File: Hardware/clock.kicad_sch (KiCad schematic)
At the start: 0 parts

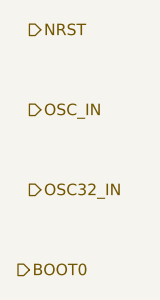
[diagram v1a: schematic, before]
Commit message: Add fast clock
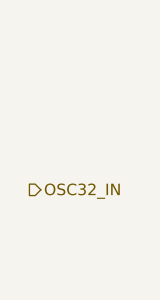
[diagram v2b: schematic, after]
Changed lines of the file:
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@@
 	(generator_version "9.0")
 	(paper "A4")
-	(hierarchical_label "NRST"
-		(shape output)
-		(at 143.51 80.01 0)
-		(effects
-			(font
-				(size 1.27 1.27)
-			)
-			(justify left)
-		)
-	)
-	(hierarchical_label "OSC_IN"
-		(shape output)
-		(at 143.51 88.9 0)
-		(effects
-			(font
-				(size 1.27 1.27)
-			)
-			(justify left)
-		)
-	)
 	(hierarchical_label "OSC32_IN"
 		(shape output)
@@
 		(effects
 			(font
-				(size 1.27 1.27)
-			)
-			(justify left)
-		)
-	)
-	(hierarchical_label "BOOT0"
-		(shape output)
-		(at 142.24 106.68 0)
-		(effects
-			(font
